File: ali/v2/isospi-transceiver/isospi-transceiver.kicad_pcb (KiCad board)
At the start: 4 copper layers, 52 x 76 mm, 77 parts, among them J1 Conn_02x01, J2 Conn_01x05, J3 USB_C_Receptacle_USB2.0_16P, J4 Conn_01x06, J6 Screw_Terminal_01x02, J7 Conn_01x03, J8 Vertical Ethernet, SW1 SKRPANE010, U1 STM32H563RIV6, U2 AP2112K-3.3, U3 TJA1462ATK, U4 LAN8742AI, U5 ADBMS6821, U6 UCC33420-Q1, Y1 25 MHz, Y2 25 MHz

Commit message: Big changes (Tim and Daniel review part 1)
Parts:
- H1, H2, H3, H4: footprint MountingHole:MountingHole_3.2mm_M3 -> APRL_Misc:MountingHole_3.2mm_M3
- J6: footprint Connector_Phoenix_MSTB:PhoenixContact_MSTBV_2,5_2-GF-5,08_1x02_P5.08mm_Vertical_ThreadedFlange_MountHole -> APRL_Connector:PhoenixContact_MSTBV_2,5_2-GF-5,08_1x02_P5.08mm_Vertical_ThreadedFlange_MountHole
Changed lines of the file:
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@@
 			(drill 0.889)
 			(layers "*.Cu" "*.Mask")
+			(clearance 0.8)
 		)
 		(pad "1" thru_hole circle
@@
 			)
 		)
+		(zone_connect 2)
 		(attr smd)
 		(duplicate_pad_numbers_are_jumpers no)
@@
 		)
 	)
-	(footprint "MountingHole:MountingHole_3.2mm_M3"
+	(footprint "APRL_Misc:MountingHole_3.2mm_M3"
 		(layer "F.Cu")
 		(at 162.7125 134.325)
@@
 			(drill 3.2)
 			(layers "*.Cu" "*.Mask")
+			(clearance 0.8)
 		)
 		(embedded_fonts no)
@@
 			)
 		)
+		(zone_connect 2)
 		(attr smd)
 		(duplicate_pad_numbers_are_jumpers no)
@@
 			)
 		)
+		(zone_connect 2)
 		(attr smd)
 		(duplicate_pad_numbers_are_jumpers no)
@@
 		)
 	)
-	(footprint "MountingHole:MountingHole_3.2mm_M3"
+	(footprint "APRL_Misc:MountingHole_3.2mm_M3"
 		(layer "F.Cu")
 		(at 162.7125 68.325)
@@
 			(drill 3.2)
 			(layers "*.Cu" "*.Mask")
+			(clearance 0.8)
 		)
 		(embedded_fonts no)
@@
 		)
 	)
-	(footprint "MountingHole:MountingHole_3.2mm_M3"
+	(footprint "APRL_Misc:MountingHole_3.2mm_M3"
 		(layer "F.Cu")
 		(at 120.7125 68.325)
@@
 			(drill 3.2)
 			(layers "*.Cu" "*.Mask")
+			(clearance 0.8)
 		)
 		(embedded_fonts no)
@@
 			(drill 3.2)
 			(layers "*.Cu" "*.Mask")
+			(clearance 0.8)
 		)
 		(pad "" np_thru_hole circle
@@
 			(drill 3.2)
 			(layers "*.Cu" "*.Mask")
+			(clearance 0.8)
 		)
 		(pad "1" thru_hole rect
@@
 		)
 	)
-	(footprint "MountingHole:MountingHole_3.2mm_M3"
+	(footprint "APRL_Misc:MountingHole_3.2mm_M3"
 		(layer "F.Cu")
 		(at 120.7125 134.325)
@@
 			(drill 3.2)
 			(layers "*.Cu" "*.Mask")
+			(clearance 0.8)
 		)
 		(embedded_fonts no)
@@
 			(drill 0.889)
 			(layers "*.Cu" "*.Mask")
+			(clearance 0.8)
 		)
 		(pad "1" thru_hole circle
@@
 		)
 	)
-	(footprint "Connector_Phoenix_MSTB:PhoenixContact_MSTBV_2,5_2-GF-5,08_1x02_P5.08mm_Vertical_ThreadedFlange_MountHole"
+	(footprint "APRL_Connector:PhoenixContact_MSTBV_2,5_2-GF-5,08_1x02_P5.08mm_Vertical_ThreadedFlange_MountHole"
 		(layer "F.Cu")
 		(at 158.49 80.99 -90)
@@
 			(drill 2.4)
 			(layers "*.Cu" "*.Mask")
+			(clearance 0.8)
 		)
 		(pad "" np_thru_hole circle
@@
 			(drill 2.4)
 			(layers "*.Cu" "*.Mask")
+			(clearance 0.8)
 		)
 		(pad "1" thru_hole roundrect
@@
 			)
 		)
+		(zone_connect 2)
 		(attr smd)
 		(duplicate_pad_numbers_are_jumpers no)
@@
 		(layers "F.Cu" "B.Cu" "In1.Cu" "In2.Cu")
 		(hatch edge 0.5)
-		(priority 7)
-		(connect_pads yes
-			(clearance 0.2)
-		)
-		(min_thickness 0.15)
-		(fill yes
-			(thermal_gap 0.5)
-			(thermal_bridge_width 0.5)
-			(island_removal_mode 0)
-		)
-		(polygon
-			(pts
-				(xy 147.3925 102.27483) (xy 150.1225 102.27507) (xy 150.1225 105.745) (xy 147.3925 105.745)
-			)
-		)
-	)
-	(zone
-		(net "GND")
-		(layers "F.Cu" "B.Cu" "In1.Cu" "In2.Cu")
-		(hatch edge 0.5)
 		(connect_pads thru_hole_only
 			(clearance 0.2)
 		)
 		(min_thickness 0.15)
-		(fill
+		(fill yes
 			(thermal_gap 0.5)
 			(thermal_bridge_width 0.5)
@@
 	)
 	(zone
-		(net "GND")
-		(layers "F.Cu" "B.Cu" "In1.Cu" "In2.Cu")
-		(hatch edge 0.5)
-		(priority 9)
-		(connect_pads yes
-			(clearance 0.2)
-		)
-		(min_thickness 0.15)
-		(fill yes
-			(thermal_gap 0.5)
-			(thermal_bridge_width 0.5)
-			(island_removal_mode 0)
-		)
-		(polygon
-			(pts
-				(xy 131.6125 119.975) (xy 135.0125 119.975) (xy 135.0125 123.425) (xy 131.6125 123.383025)
-			)
-		)
-	)
-	(zone
-		(net "GND")
-		(layers "F.Cu" "B.Cu" "In1.Cu" "In2.Cu")
-		(hatch edge 0.5)
-		(priority 6)
-		(connect_pads yes
-			(clearance 0.2)
-		)
-		(min_thickness 0.15)
-		(fill yes
-			(thermal_gap 0.5)
-			(thermal_bridge_width 0.5)
-			(island_removal_mode 0)
-		)
-		(polygon
-			(pts
-				(xy 128.9125 95.025) (xy 136.6125 95.025) (xy 136.6125 102.625) (xy 128.9125 102.625)
-			)
-		)
-	)
-	(zone
 		(net "+5V")
 		(layer "B.Cu")
@@
 			)
 		)
-	)
-	(zone
-		(net "GND")
-		(layers "B.Cu" "In1.Cu" "In2.Cu")
-		(hatch edge 0.5)
-		(priority 10)
-		(connect_pads yes
-			(clearance 0.09)
-		)
-		(min_thickness 0.15)
-		(fill yes
-			(thermal_gap 0.5)
-			(thermal_bridge_width 0.5)
-			(island_removal_mode 0)
-		)
-		(polygon
-			(pts
-				(xy 129.5125 95.775) (xy 135.8625 95.775) (xy 135.8625 102.125) (xy 129.5125 102.125)
-			)
-		)

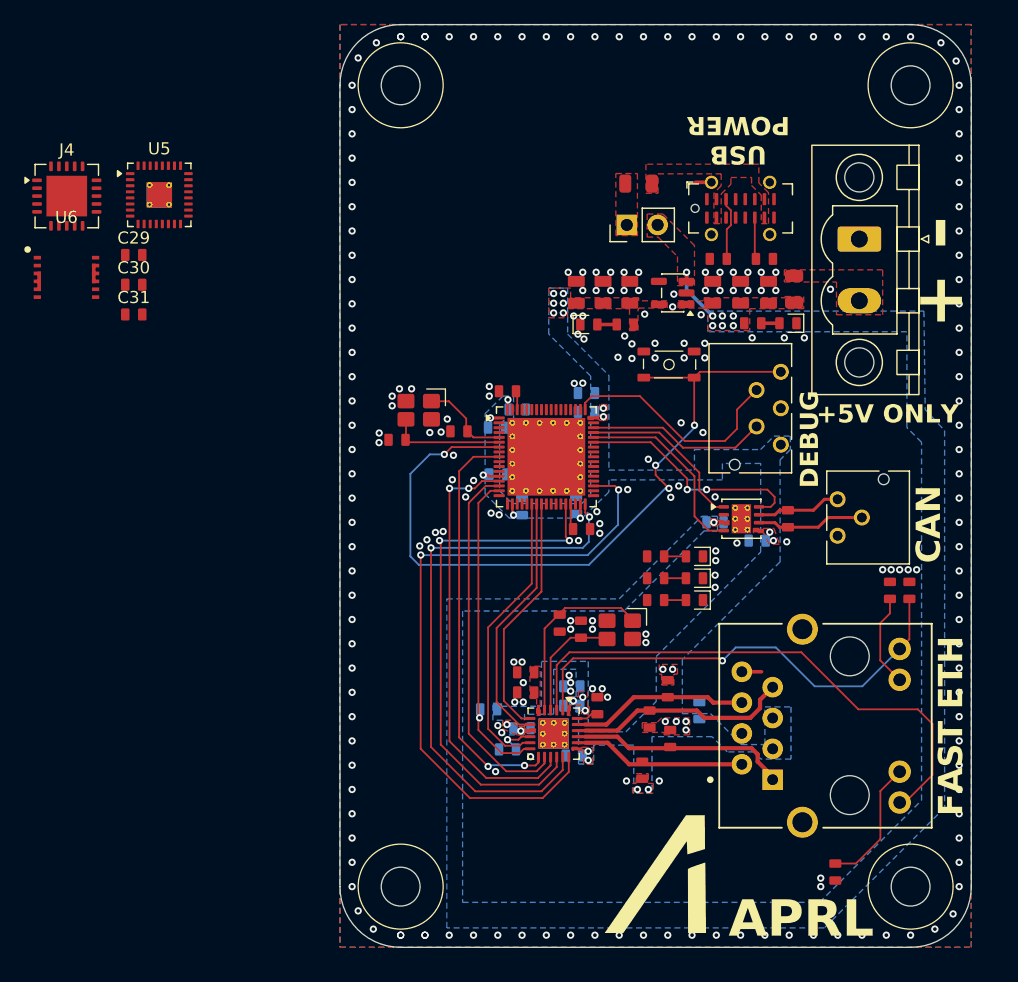
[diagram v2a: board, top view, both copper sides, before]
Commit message: Use 1206 on AFEs
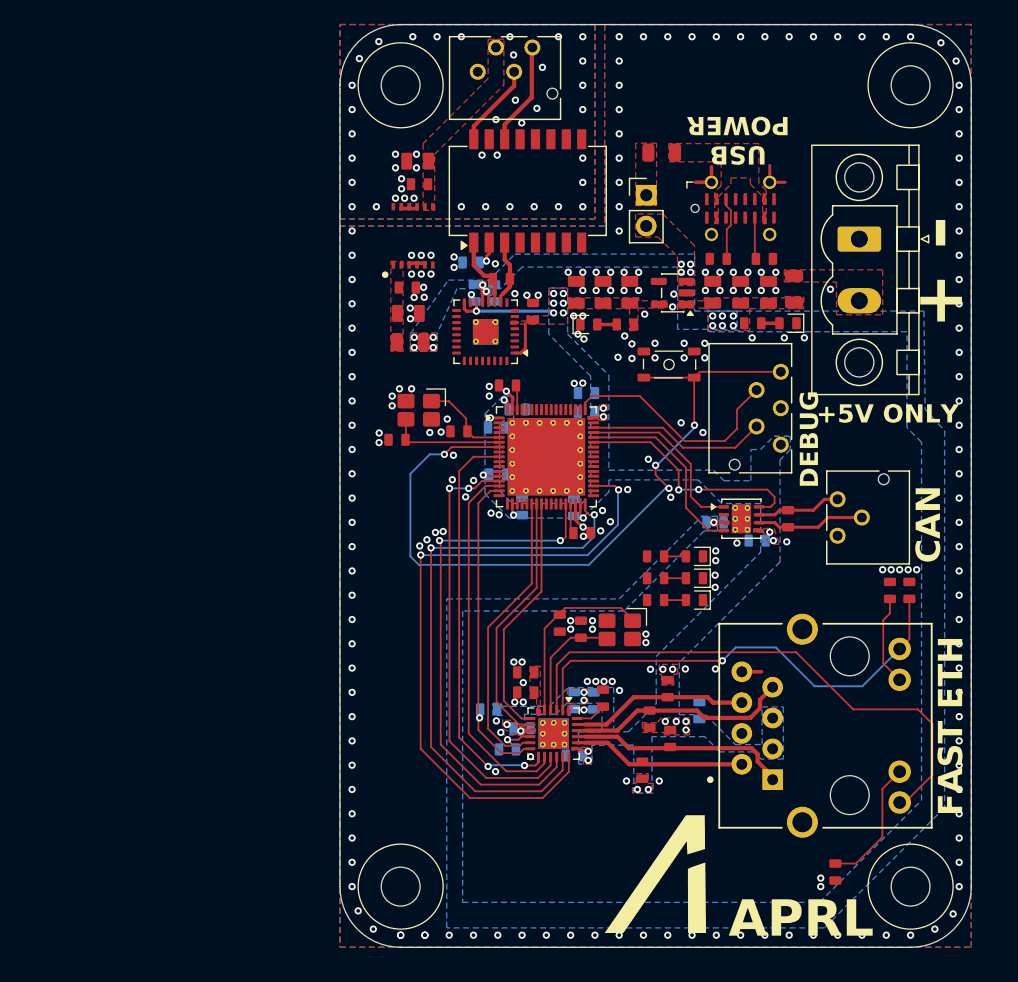
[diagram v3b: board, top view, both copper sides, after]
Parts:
- removed the J4 at (93.2, 77.5)
- added C32: 10nF, APRL_Passive:C_0603, B.Cu at (126.5, 82.9)
- added C33: 22uF, APRL_Passive:C_0805, F.Cu at (121.4, 87.1)
- added C34: 10nF, APRL_Passive:C_0603, F.Cu at (121.3, 85.0)
- added C35: 10nF, APRL_Passive:C_0603, F.Cu at (122.3, 76.5)
- added C36: 22uF, APRL_Passive:C_0805, F.Cu at (122.1, 74.6)
- added F3: 500mA, APRL_Passive:Fuse_0805_2012Metric, F.Cu at (121.5, 89.5)
- added J7: Conn_01x04, APRL_Connector_Molex:Molex_CLIK-Mate_503159-0401_1x04-1MP_P1.50mm_Vertical, F.Cu at (131.6, 65.2)
- added R19: 100R, APRL_Passive:R_0603, F.Cu at (129.0, 84.3)
- added TR1: HX1188NL, APRL_Passive:Transformer_Ethernet_Pulse_HX1188NL_SO-16_7.11x12.7mm, F.Cu at (131.2, 77.0)
- C30, C31: moved to B.Cu
- moved C29 33.2 mm to (131.6, 87.0), turned to 90 degrees
- moved C31 29.7 mm to (128.4, 85.4), turned to -90 degrees
- moved U5 29.1 mm to (127.7, 88.6), turned to 180 degrees
- moved U6 28.8 mm to (121.7, 80.7), turned to 90 degrees
- moved C30 28.1 mm to (126.8, 85.4), turned to -90 degrees
- moved F1 3.18 mm to (142.2, 73.9)
- moved J1 2.93 mm to (140.9, 77.4), turned to 0 degrees
- moved C18 2.16 mm to (136.6, 119.0), turned to -90 degrees
- moved R14 0.79 mm to (137.4, 118.8)
- moved C11 0.48 mm to (129.5, 93.0)
- moved C28 0.47 mm to (135.0, 119.0), turned to -90 degrees
- moved C10 0.33 mm to (135.6, 105.2)
- moved C5 0.25 mm to (135.0, 103.1)
- renumbered C20 to C19, C21 to C20, C25 to C21, C23 to C22, C24 to C23, C26 to C24, C27 to C25, C28 to C26, C22 to C27, C19 to C28, J6 to J4, J8 to J5, J7 to J6, R11 to R10, R12 to R11, R13 to R12, R14 to R13, R15 to R14, R16 to R15, R17 to R16, R18 to R17, R8 to R18, R9 to R8, R10 to R9, U4 to U3, U3 to U4
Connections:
- net /Connectivity/CAN+ renamed Net-(J6-Pin_1)
- net /Connectivity/CAN- renamed Net-(J6-Pin_2)
- net /Connectivity/LED1-REGOFF renamed Net-(U3-LED1/REGOFF)
- net /Connectivity/LED2-INTSEL renamed Net-(U3-LED2/~{INTSEL})
- net /Connectivity/RX+ renamed Net-(J5-RD+)
- net /Connectivity/RX- renamed Net-(J5-RD-)
- net /Connectivity/TX+ renamed Net-(J5-TD+)
- net /Connectivity/TX- renamed Net-(J5-TD-)
- net Net-(U6-GNDS-Pad10) renamed GNDPWR
- U5 pad 10: unconnected-(U5-IM-Pad10) -> Net-(TR1-TD-)
- U5 pad 11: unconnected-(U5-IP-Pad11) -> Net-(TR1-TD+)
- U5 pad 14: unconnected-(U5-PHAPOL-Pad14) -> +3.3V
- U5 pad 15: unconnected-(U5-RTO-Pad15) -> GND
- U5 pad 16: unconnected-(U5-XCVRMD-Pad16) -> +3.3V
- U5 pad 2: unconnected-(U5-PICO-Pad2) -> /isoSPI/MISO
- U5 pad 3: unconnected-(U5-POCI-Pad3) -> /isoSPI/MOSI
- U5 pad 4: unconnected-(U5-SCK-Pad4) -> /isoSPI/SCK
- U5 pad 5: unconnected-(U5-~{CS}-Pad5) -> /isoSPI/~{CS}
- U5 pad 7: /isoSPI/INT -> unconnected-(U5-INTR-Pad7)
- U6 pad 1: unconnected-(U6-EN/FLT-Pad1) -> Net-(U6-EN/FLT)
- U6 pad 2: unconnected-(U6-VINP-Pad2) -> Net-(U6-EN/FLT)
- U6 pad 3: Net-(U6-GNDP-Pad3) -> GND
- U6 pad 4: Net-(U6-GNDP-Pad3) -> GND
- U6 pad 5: Net-(U6-GNDP-Pad3) -> GND
- U6 pad 6: Net-(U6-GNDP-Pad3) -> GND
- U6 pad 7: unconnected-(U6-SEL-Pad7) -> Net-(J7-Pin_3)
- U6 pad 8: unconnected-(U6-VCC-Pad8) -> Net-(J7-Pin_3)
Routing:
- net +3.3V: track 5.21 -> 17.4 mm
- net Net-(J7-Pin_1): track 0.00 -> 8.50 mm
- net GND: track 2.94 -> 10.8 mm, vias 239 -> 248
- net Net-(J7-Pin_2): track 0.00 -> 6.94 mm
- net Net-(TR1-TD+): track 0.00 -> 5.92 mm
- net Net-(TR1-TD-): track 0.00 -> 5.44 mm
- net +5V: track 5.23 -> 2.52 mm, vias 8 -> 17
- net Net-(TR1-TCT): track 0.00 -> 2.23 mm, vias 0 -> 1
- net Net-(U3-RBIAS): track 1.81 -> 2.54 mm
- net /Connectivity/FDCAN_TX: track 14.1 -> 14.8 mm
- net /Connectivity/ETH_TX_EN: track 43.0 -> 42.4 mm
- net /Connectivity/ETH_TXD0: track 47.0 -> 47.6 mm
- net GNDPWR: vias 0 -> 43
- added copper zone on B.Cu, net GNDPWR
- added copper zone on F.Cu, net GNDPWR
- added copper zone on In1.Cu, net GNDPWR
- added copper zone on In2.Cu, net GNDPWR
- added copper zone on F.Cu, net Net-(J7-Pin_3)
- added copper zone on F.Cu, net Net-(U6-EN/FLT)

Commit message: Simplify chickensticks, get isospi-tx ready, and update some cubemx projects
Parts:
- moved D3 0.50 mm to (144.9, 110.2)
- moved D4 0.50 mm to (144.9, 108.4)
- moved D5 0.50 mm to (144.9, 106.6)
- moved R5 0.50 mm to (141.7, 110.2)
- moved R6 0.50 mm to (141.7, 108.4)
- moved R7 0.50 mm to (141.7, 106.6)
- moved C19 0.49 mm to (130.7, 120.8)
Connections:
- U1 pad 26: unconnected-(U1-PB0-Pad26) -> /Microcontroller/USER_LED_1
- U1 pad 27: unconnected-(U1-PB1-Pad27) -> /Microcontroller/USER_LED_2
- U1 pad 35: unconnected-(U1-PB13-Pad35) -> /Microcontroller/USER_LED_3
- U1 pad 56: unconnected-(U1-PC12-Pad56) -> /Microcontroller/~{CS}
- U1 pad 57: unconnected-(U1-PB3(JTDO-Pad57) -> /Microcontroller/SCK
- U1 pad 58: unconnected-(U1-PB4(NJTRST)-Pad58) -> /Microcontroller/MISO
- U1 pad 59: unconnected-(U1-PB5-Pad59) -> /Microcontroller/MOSI
- U5 pad 2: /isoSPI/MISO -> /Microcontroller/MISO
- U5 pad 3: /isoSPI/MOSI -> /Microcontroller/MOSI
- U5 pad 4: /isoSPI/SCK -> /Microcontroller/SCK
- U5 pad 5: /isoSPI/~{CS} -> /Microcontroller/~{CS}
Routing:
- net +5V: track 2.52 -> 51.3 mm
- net /Microcontroller/USER_LED_1: track 0.00 -> 14.9 mm
- net /Microcontroller/USER_LED_2: track 0.00 -> 12.9 mm
- net /Microcontroller/~{CS}: track 0.00 -> 10.2 mm
- net /Microcontroller/SCK: track 0.00 -> 9.46 mm
- net /Microcontroller/MISO: track 0.00 -> 8.06 mm, vias 0 -> 2
- net /Microcontroller/USER_LED_3: track 0.00 -> 7.92 mm
- net /Microcontroller/MOSI: track 0.00 -> 7.87 mm
- net +3.3V: track 17.4 -> 18.8 mm, vias 30 -> 31
- net /Microcontroller/~{RST}: track 61.7 -> 60.8 mm
- net /Connectivity/FDCAN_STDBY: track 19.7 -> 18.9 mm
- net Net-(C10-Pad1): track 1.86 -> 2.48 mm
- net GNDPWR: vias 43 -> 53
- net GND: vias 248 -> 303
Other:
- board text added: "ISOSPI"
